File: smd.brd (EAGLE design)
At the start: 42.9 x 30.5 mm, 4 parts, among them J1 2.1MMJACKTHM

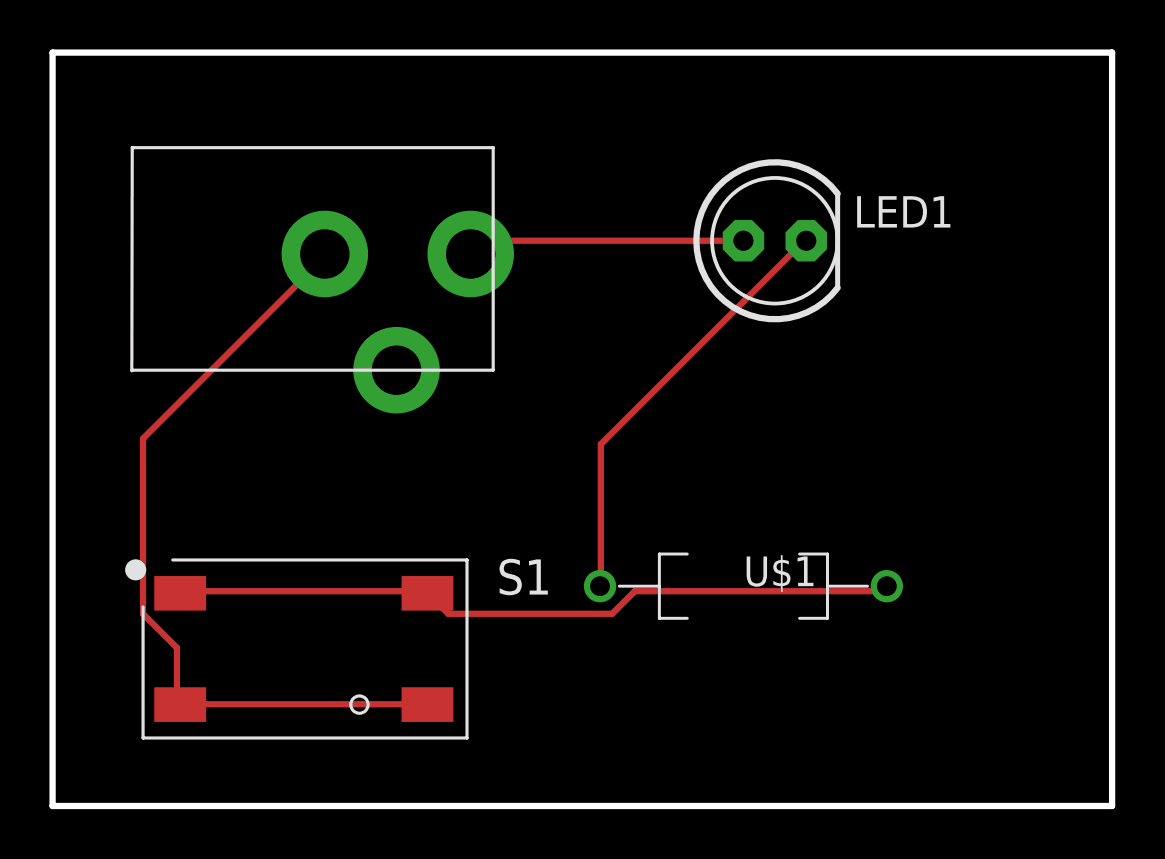
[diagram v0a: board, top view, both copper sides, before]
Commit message: Added logo to the boards.
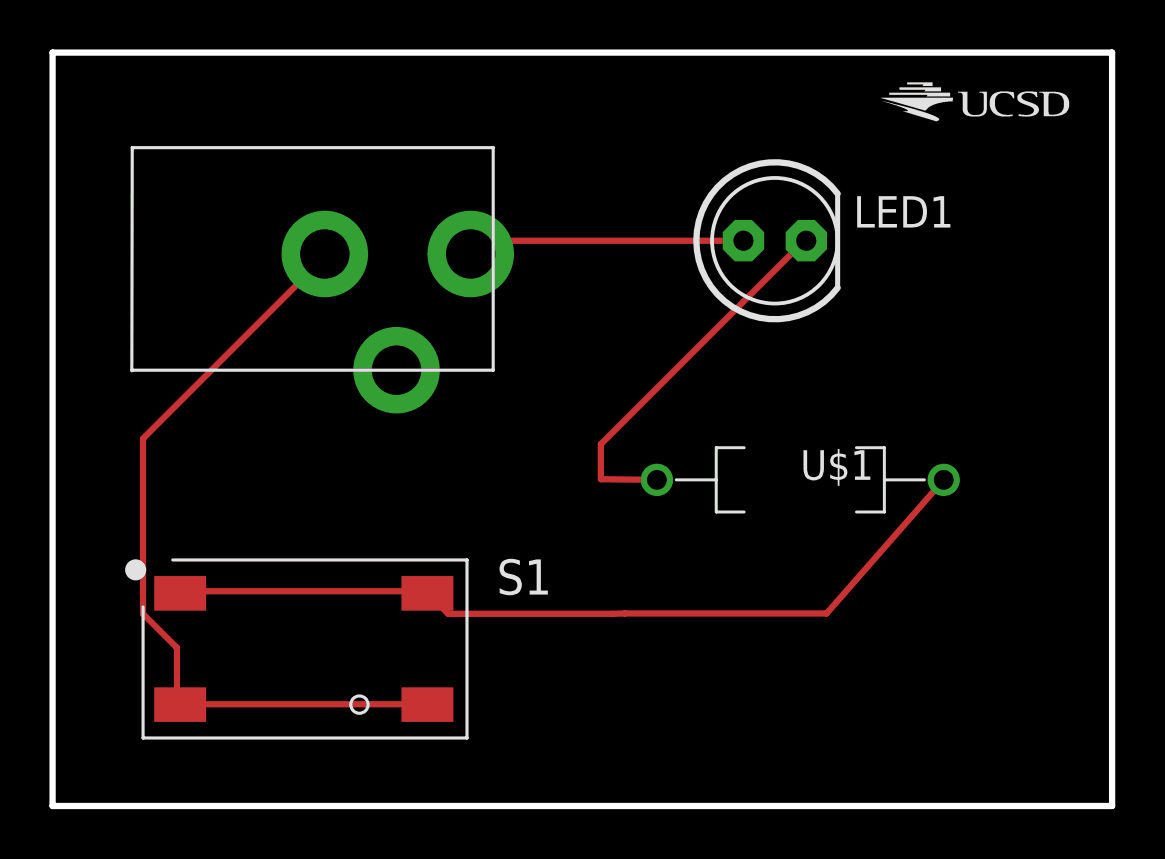
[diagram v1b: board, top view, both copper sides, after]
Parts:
- added U$2: (no value), Logos:UCSD_LOGO
- moved U$1 4.88 mm to (30.2, 13.2)
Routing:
- net N$3: track 29.5 -> 33.7 mm
- net N$2: track 17.5 -> 15.4 mm
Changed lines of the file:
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@@
 <element name="LED1" library="Lab2" package="LED5MM" value="Red" x="29.21" y="22.86"/>
 <element name="S1" library="sainan-Lab2" package="BUTTON-TACTILE-SQUARE-LSH" value="BUTTON-TACTILE-SQUARE" x="10.16" y="6.35"/>
-<element name="U$1" library="Lab2" package="RESAD1160W55L680D260_HS" value="330Ohms" x="27.94" y="8.89">
-<attribute name="DESC" value="" x="27.94" y="8.89" size="1.778" layer="27" display="off"/>
-<attribute name="PWR" value="" x="27.94" y="8.89" size="1.778" layer="27" display="off"/>
-<attribute name="SIZE" value="" x="27.94" y="8.89" size="1.778" layer="27" display="off"/>
-<attribute name="TOL" value="" x="27.94" y="8.89" size="1.778" layer="27" display="off"/>
-<attribute name="URL" value="" x="27.94" y="8.89" size="1.778" layer="27" display="off"/>
-<attribute name="MFR" value="" x="27.94" y="8.89" size="1.778" layer="27" display="off"/>
-<attribute name="MPN" value="" x="27.94" y="8.89" size="1.778" layer="27" display="off"/>
-<attribute name="DIST1" value="" x="27.94" y="8.89" size="1.778" layer="27" display="off"/>
-<attribute name="CASE" value="" x="27.94" y="8.89" size="1.778" layer="27" display="off"/>
-<attribute name="DIST1PN" value="" x="27.94" y="8.89" size="1.778" layer="27" display="off"/>
-<attribute name="VAL" value="" x="27.94" y="8.89" size="1.778" layer="27" display="off"/>
+<element name="U$1" library="Lab2" package="RESAD1160W55L680D260_HS" value="330Ohms" x="30.24" y="13.19">
+<attribute name="DESC" value="" x="30.24" y="13.19" size="1.778" layer="27" display="off"/>
+<attribute name="PWR" value="" x="30.24" y="13.19" size="1.778" layer="27" display="off"/>
+<attribute name="SIZE" value="" x="30.24" y="13.19" size="1.778" layer="27" display="off"/>
+<attribute name="TOL" value="" x="30.24" y="13.19" size="1.778" layer="27" display="off"/>
+<attribute name="URL" value="" x="30.24" y="13.19" size="1.778" layer="27" display="off"/>
+<attribute name="MFR" value="" x="30.24" y="13.19" size="1.778" layer="27" display="off"/>
+<attribute name="MPN" value="" x="30.24" y="13.19" size="1.778" layer="27" display="off"/>
+<attribute name="DIST1" value="" x="30.24" y="13.19" size="1.778" layer="27" display="off"/>
+<attribute name="CASE" value="" x="30.24" y="13.19" size="1.778" layer="27" display="off"/>
+<attribute name="DIST1PN" value="" x="30.24" y="13.19" size="1.778" layer="27" display="off"/>
+<attribute name="VAL" value="" x="30.24" y="13.19" size="1.778" layer="27" display="off"/>
 </element>
+<element name="U$2" library="Logos" package="UCSD_LOGO" value="" x="33.5" y="27.7"/>
 </elements>
 <signals>
@@
 <contactref element="LED1" pad="K"/>
 <contactref element="U$1" pad="1"/>
-<wire x1="22.1742" y1="14.6304" x2="22.1742" y2="8.9154" width="0.254" layer="1"/>
+<wire x1="22.1742" y1="14.6304" x2="22.1742" y2="13.2154" width="0.254" layer="1"/>
 <wire x1="30.4038" y1="22.86" x2="22.1742" y2="14.6304" width="0.254" layer="1"/>
-<wire x1="22.1742" y1="8.9154" x2="22.14" y2="8.89" width="0.254" layer="1"/>
+<wire x1="22.1742" y1="13.2154" x2="24.44" y2="13.19" width="0.254" layer="1"/>
 <wire x1="30.4038" y1="22.86" x2="30.48" y2="22.86" width="0.254" layer="1"/>
 </signal>
@@
 <wire x1="5.2578" y1="8.6868" x2="5.16" y2="8.6" width="0.254" layer="1"/>
 <wire x1="15.0876" y1="8.6868" x2="15.16" y2="8.6" width="0.254" layer="1"/>
-<wire x1="23.5458" y1="8.6868" x2="33.6042" y2="8.6868" width="0.254" layer="1"/>
-<wire x1="22.6314" y1="7.7724" x2="23.5458" y2="8.6868" width="0.254" layer="1"/>
+<wire x1="23.1458" y1="7.7868" x2="31.3042" y2="7.7868" width="0.254" layer="1"/>
+<wire x1="22.6314" y1="7.7724" x2="23.1458" y2="7.7868" width="0.254" layer="1"/>
 <wire x1="16.002" y1="7.7724" x2="22.6314" y2="7.7724" width="0.254" layer="1"/>
 <wire x1="15.3162" y1="8.4582" x2="16.002" y2="7.7724" width="0.254" layer="1"/>
-<wire x1="33.6042" y1="8.6868" x2="33.74" y2="8.89" width="0.254" layer="1"/>
+<wire x1="31.3042" y1="7.7868" x2="36.04" y2="13.19" width="0.254" layer="1"/>
 <wire x1="15.3162" y1="8.4582" x2="15.16" y2="8.6" width="0.254" layer="1"/>
 </signal>
